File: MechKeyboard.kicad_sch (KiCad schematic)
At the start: 15 parts, among them SW1 SW_Push, U1 ATmega32U4-A, Y1 16MHz

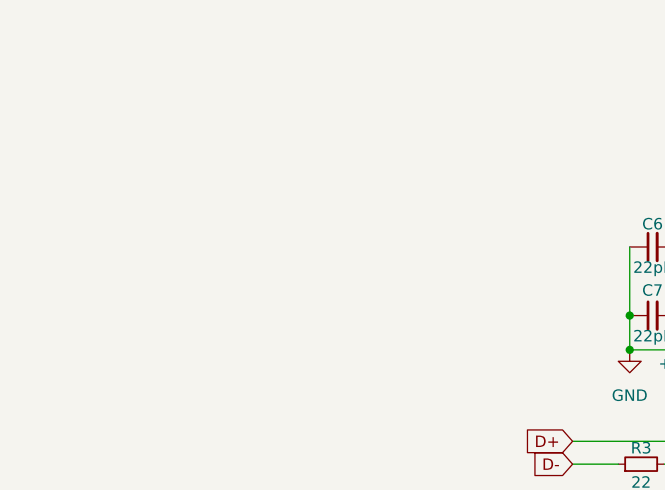
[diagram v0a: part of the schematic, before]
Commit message: USB Added
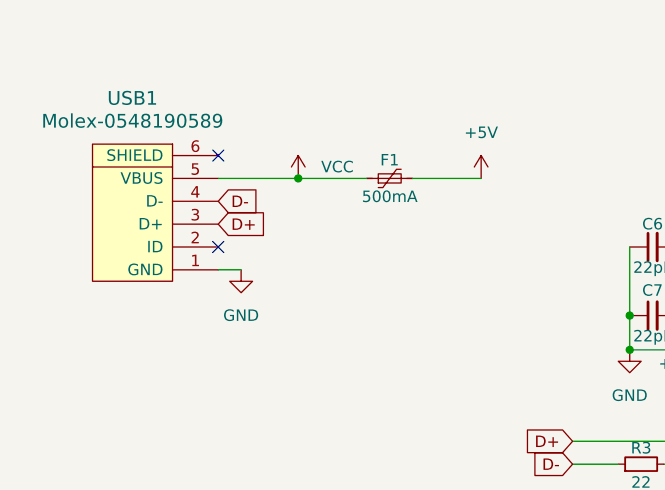
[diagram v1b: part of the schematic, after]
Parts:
- added F1: 500mA, symbol Device:Polyfuse_Small
- added USB1: Molex-0548190589, symbol keyboard-parts:Molex-0548190589
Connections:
- net +5V: now also F1.2
- net D+: now also USB1.3 (D+)
- net D-: now also USB1.4 (D-)
- net GND: now also USB1.1 (GND)
- new net VCC: F1.1, USB1.5 (VBUS)
- no-connect marks 1 -> 3
